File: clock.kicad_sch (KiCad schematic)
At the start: 19 parts, among them Q3 DTC014TEBTL, U7 NB3L202KMNTXG, U8 SN65LVDS1DR, U9 XLL736027.000000X, Y1 NX3241E0100.000000, Y2 ECS-2520MVLC-260-CM-TR, Y3 AX3DAF1-125.0000

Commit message: Bump date and revision
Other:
- title: Clock distribution -> Kria K26 Devboard
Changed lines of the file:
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@@
   (paper "A4")
   (title_block
-    (title "Clock distribution")
-    (date "2022-07-25")
-    (rev "1.1.0")
+    (title "Kria K26 Devboard")
+    (date "2023-02-15")
+    (rev "1.1.1")
     (comment 1 "www.antmicro.com")
     (comment 2 "Antmicro Ltd.")

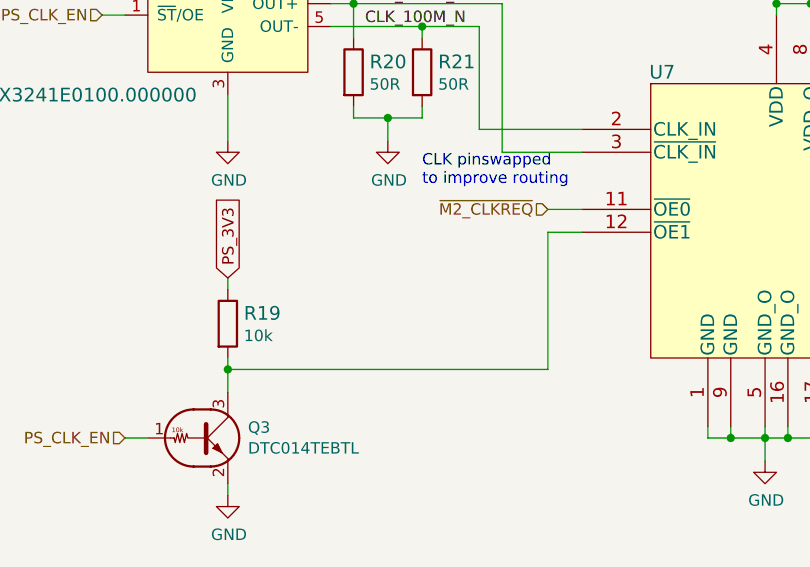
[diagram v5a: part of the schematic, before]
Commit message: Fix swapped OE signals on 100MHz PCIe clock generator
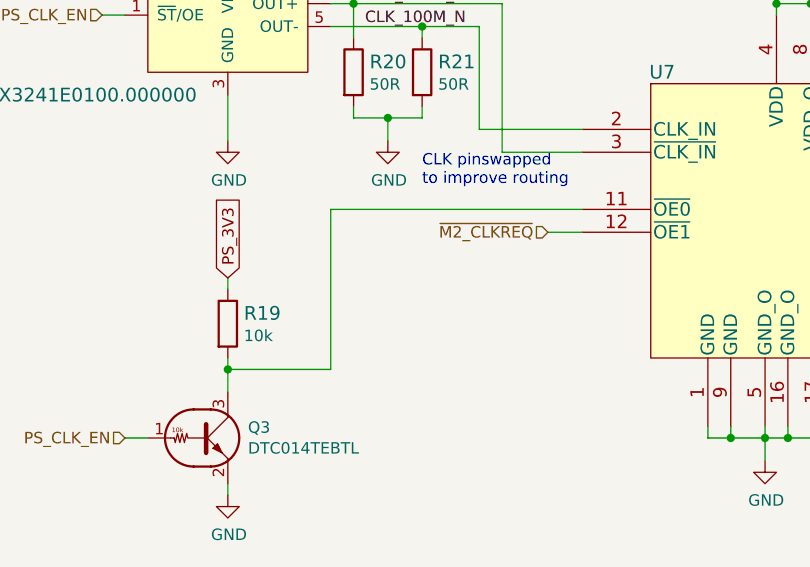
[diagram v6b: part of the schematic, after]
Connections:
- net ~{M2_CLKREQ}: now also U7.12 (~{OE1}); no longer U7.11 (~{OE0})
- net at Q3.3 (C), R19.2: now also U7.11 (~{OE0}); no longer U7.12 (~{OE1})
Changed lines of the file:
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@@
     (stroke (width 0) (type default) (color 0 0 0 0))
   )
-  (wire (pts (xy 80.01 96.52) (xy 80.01 81.28))
+  (wire (pts (xy 55.88 78.74) (xy 55.88 96.52))
     (stroke (width 0) (type default) (color 0 0 0 0))
   )
@@
     (stroke (width 0) (type default) (color 0 0 0 0))
   )
+  (wire (pts (xy 83.82 78.74) (xy 55.88 78.74))
+    (stroke (width 0) (type default) (color 0 0 0 0))
+  )
+  (wire (pts (xy 80.01 81.28) (xy 83.82 81.28))
+    (stroke (width 0) (type default) (color 0 0 0 0))
+  )
   (wire (pts (xy 132.08 159.766) (xy 138.43 159.766))
     (stroke (width 0) (type default) (color 0 0 0 0))
@@
     (stroke (width 0) (type default) (color 0 0 0 0))
   )
-  (wire (pts (xy 80.01 81.28) (xy 83.82 81.28))
-    (stroke (width 0) (type default) (color 0 0 0 0))
-  )
   (wire (pts (xy 129.54 163.576) (xy 132.08 163.576))
     (stroke (width 0) (type default) (color 0 0 0 0))
@@
     (stroke (width 0) (type default) (color 0 0 0 0))
   )
-  (wire (pts (xy 44.45 96.52) (xy 80.01 96.52))
+  (wire (pts (xy 44.45 96.52) (xy 55.88 96.52))
     (stroke (width 0) (type default) (color 0 0 0 0))
   )
@@
   )
   (wire (pts (xy 74.93 161.036) (xy 76.2 161.036))
-    (stroke (width 0) (type default) (color 0 0 0 0))
-  )
-  (wire (pts (xy 80.01 78.74) (xy 83.82 78.74))
     (stroke (width 0) (type default) (color 0 0 0 0))
   )
@@
     (effects (font (size 1.27 1.27)) (justify left))
   )
-  (hierarchical_label "~{M2_CLKREQ}" (shape input) (at 80.01 78.74 180)
+  (hierarchical_label "~{M2_CLKREQ}" (shape input) (at 80.01 81.28 180)
     (effects (font (size 1.27 1.27)) (justify right))
   )

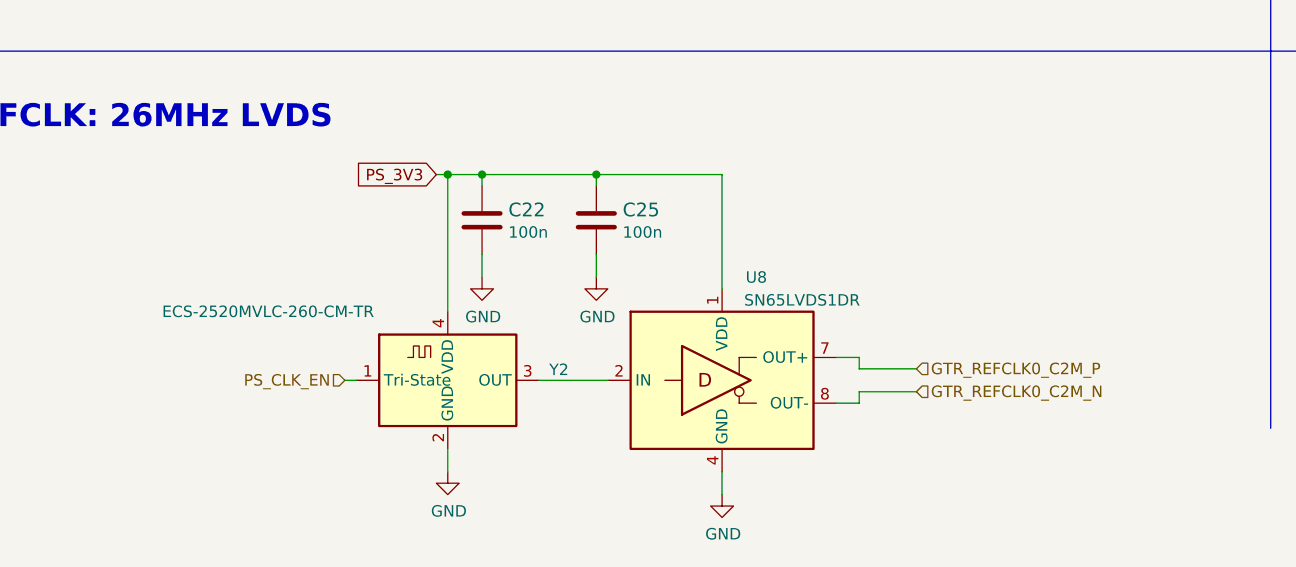
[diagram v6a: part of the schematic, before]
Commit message: Add optional pulldown for 26MHz LVDS oscillator output
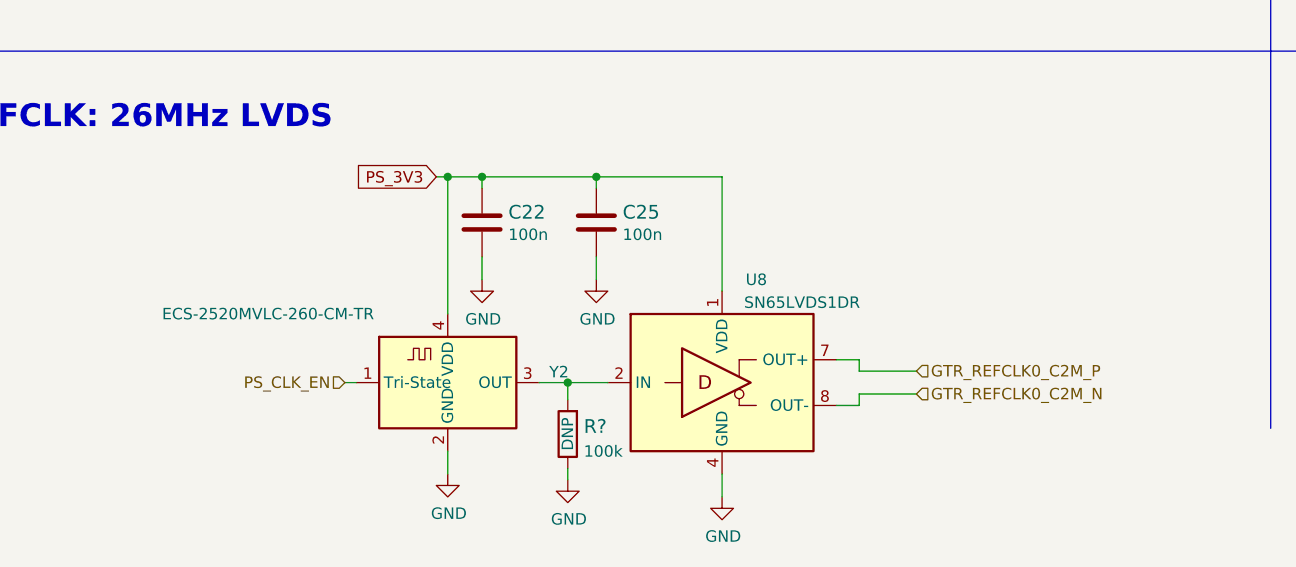
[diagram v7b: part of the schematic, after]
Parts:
- added R?: R_100k_0402, antmicro-footprints:0402-res, symbol antmicroResistors0402:R_100k_0402
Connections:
- net GND: now also R?.1
- net at U8.2 (IN), Y2.3 (OUT): now also R?.2

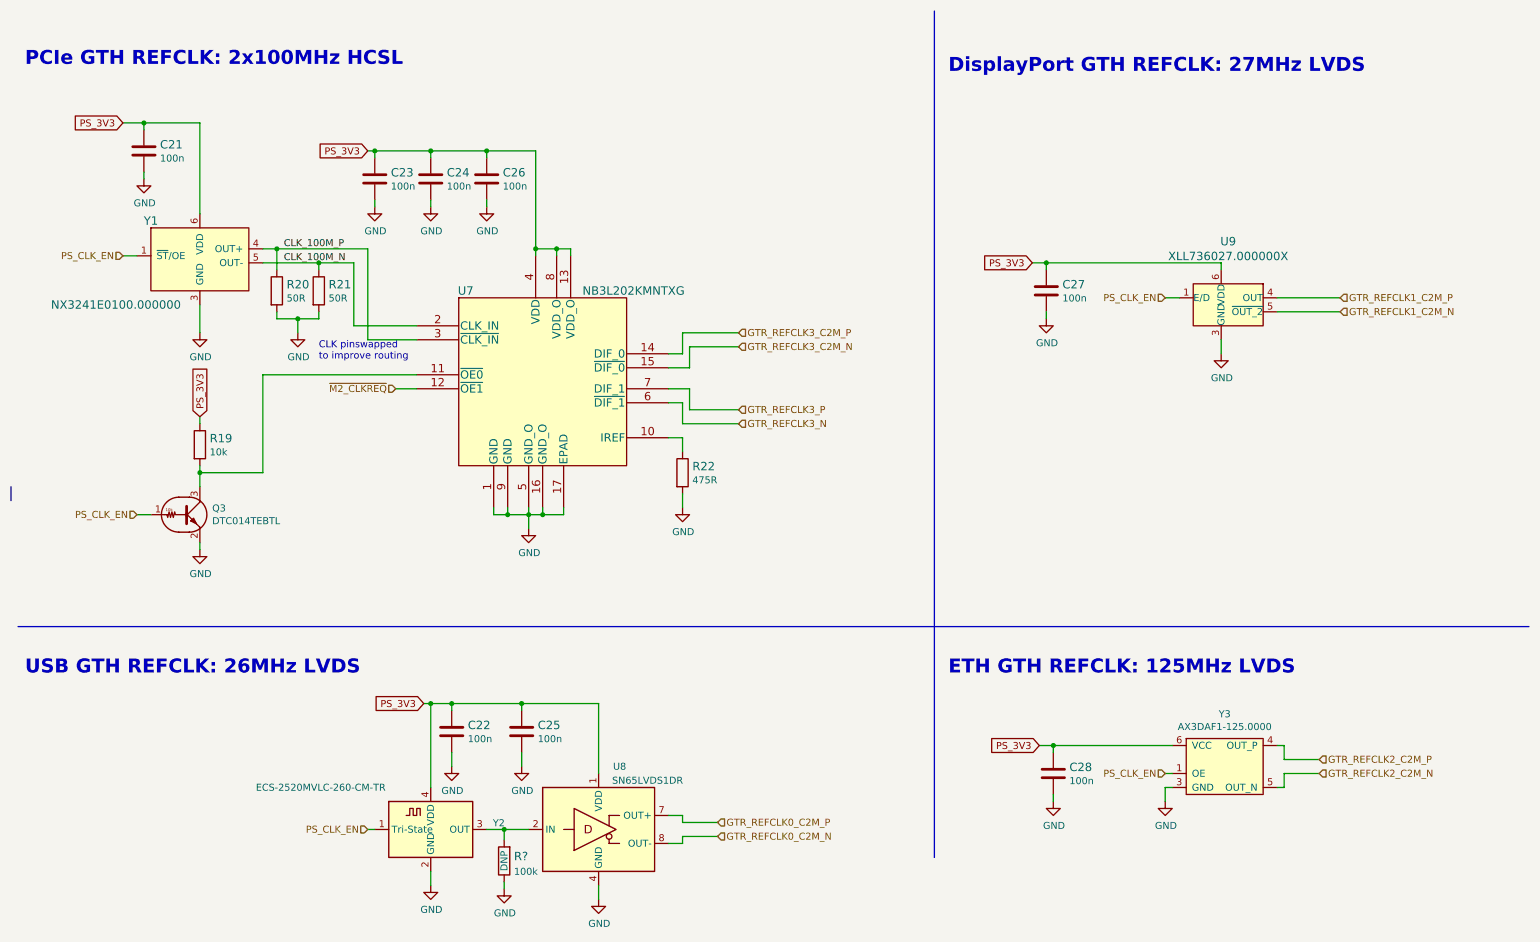
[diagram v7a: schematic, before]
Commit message: Fix TX/RX cross on M.2 Key E
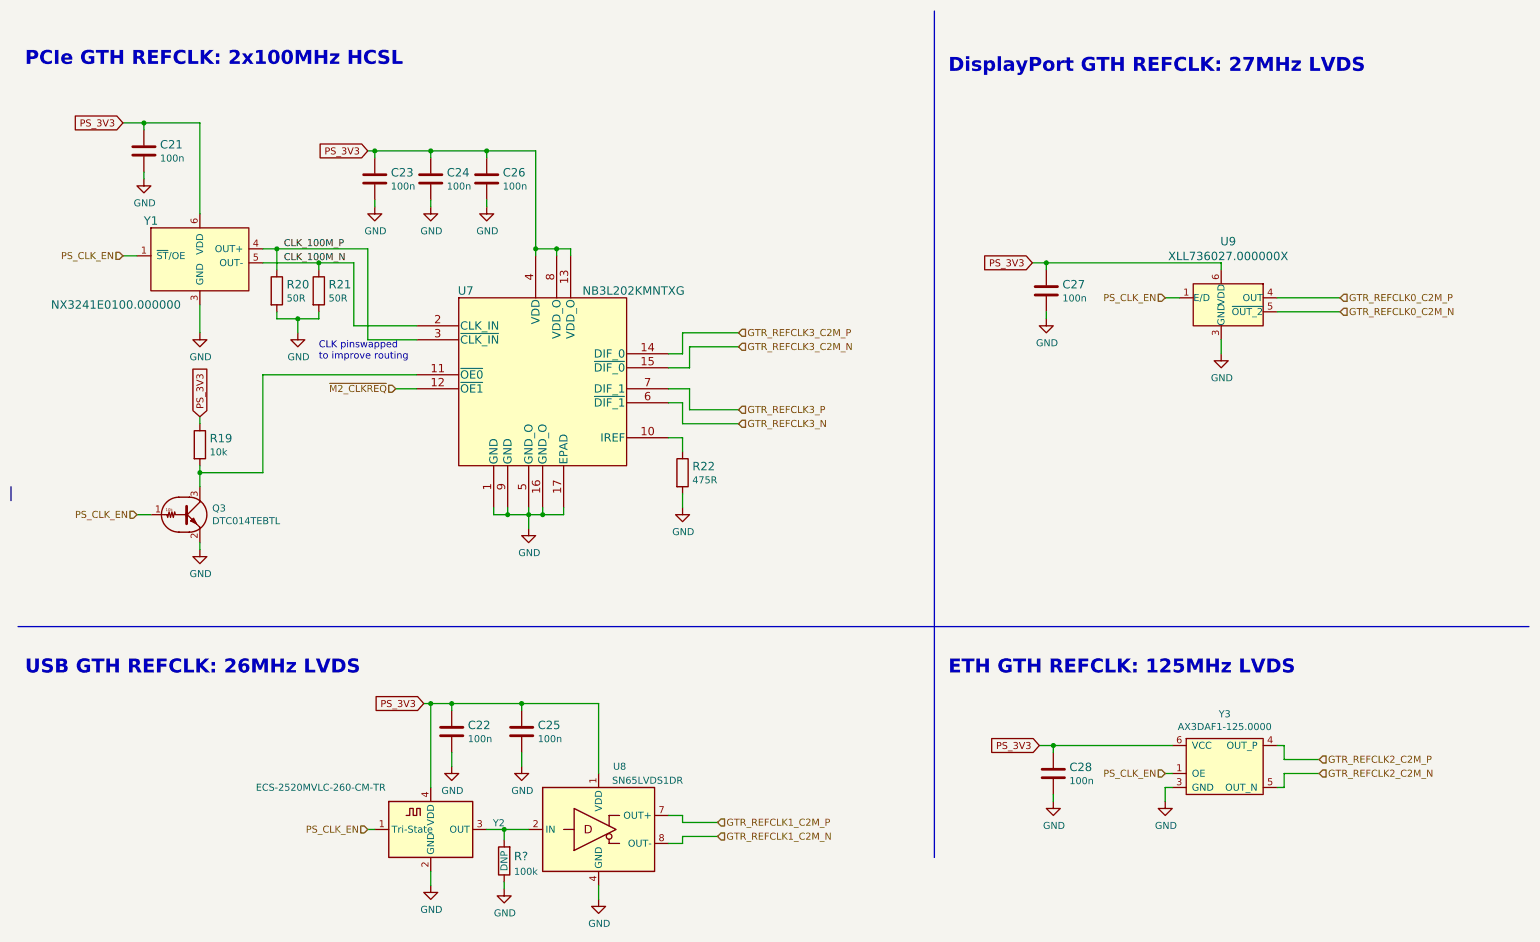
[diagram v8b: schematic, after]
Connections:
- net GTR_REFCLK0_C2M_N: now also U9.5 (~{OUT_2}); no longer U8.8 (OUT-)
- net GTR_REFCLK0_C2M_P: now also U9.4 (OUT); no longer U8.7 (OUT+)
- net GTR_REFCLK1_C2M_N: now also U8.8 (OUT-); no longer U9.5 (~{OUT_2})
- net GTR_REFCLK1_C2M_P: now also U8.7 (OUT+); no longer U9.4 (OUT)
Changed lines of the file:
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@@
     )
   )
-  (hierarchical_label "GTR_REFCLK1_C2M_N" (shape input) (at 251.46 67.31 0)
+  (hierarchical_label "GTR_REFCLK1_C2M_N" (shape input) (at 138.43 162.56 0)
     (effects (font (size 1.27 1.27)) (justify left))
   )
@@
     (effects (font (size 1.27 1.27)) (justify left))
   )
-  (hierarchical_label "GTR_REFCLK1_C2M_P" (shape input) (at 251.46 64.77 0)
+  (hierarchical_label "GTR_REFCLK1_C2M_P" (shape input) (at 138.43 160.02 0)
     (effects (font (size 1.27 1.27)) (justify left))
   )
@@
     (effects (font (size 1.27 1.27)) (justify right))
   )
-  (hierarchical_label "GTR_REFCLK0_C2M_P" (shape input) (at 138.43 160.02 0)
+  (hierarchical_label "GTR_REFCLK0_C2M_P" (shape input) (at 251.46 64.77 0)
     (effects (font (size 1.27 1.27)) (justify left))
   )
@@
     (effects (font (size 1.27 1.27)) (justify left))
   )
-  (hierarchical_label "GTR_REFCLK0_C2M_N" (shape input) (at 138.43 162.56 0)
+  (hierarchical_label "GTR_REFCLK0_C2M_N" (shape input) (at 251.46 67.31 0)
     (effects (font (size 1.27 1.27)) (justify left))
   )
